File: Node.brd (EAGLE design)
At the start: 27.9 x 27.9 mm, 60 parts, among them J1 DF12A3.0-14DS, Q1 16MHz, U1 ATMEGA32U4QFN, U2 NRF24L01NOPAD, U3 LTC3553, U4 L3GD20, U6 LSM303DLHC, U7 BD2425NNRF0404, U9 RCLAMP0502A, X1 USB-FCI

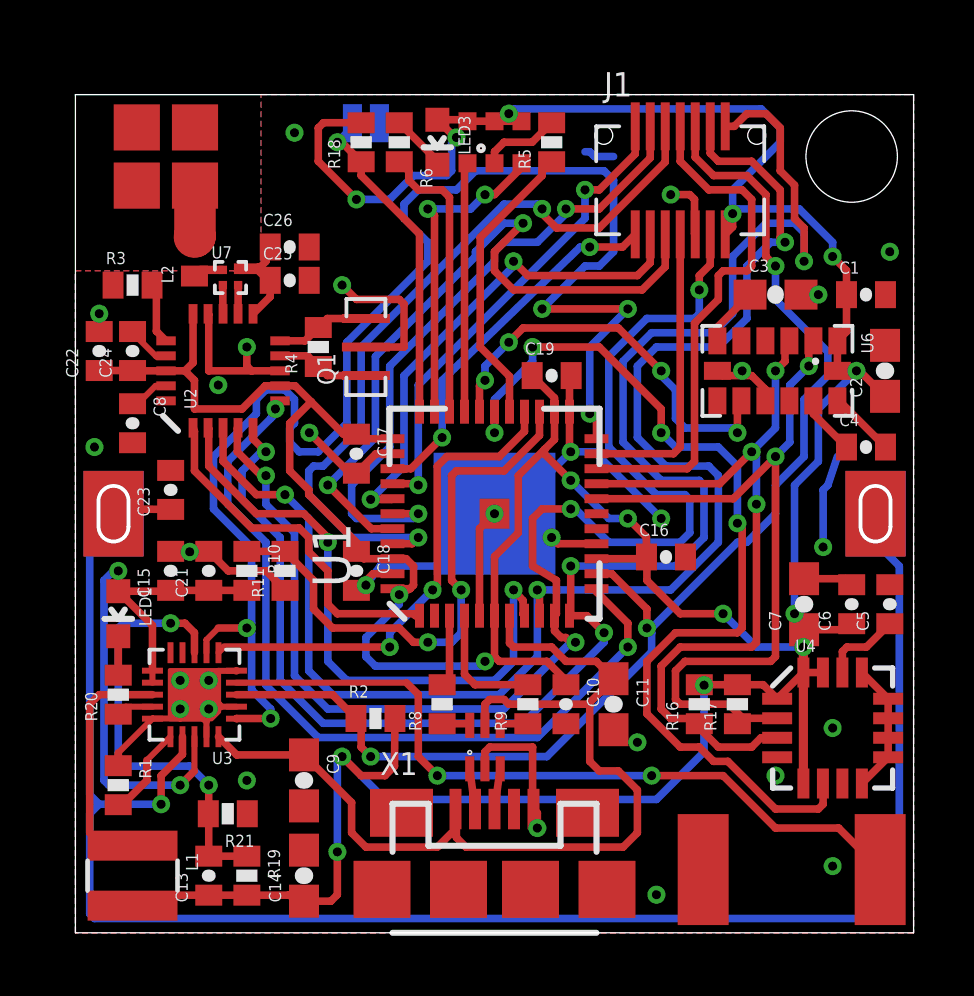
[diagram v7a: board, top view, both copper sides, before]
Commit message: with silkscreen
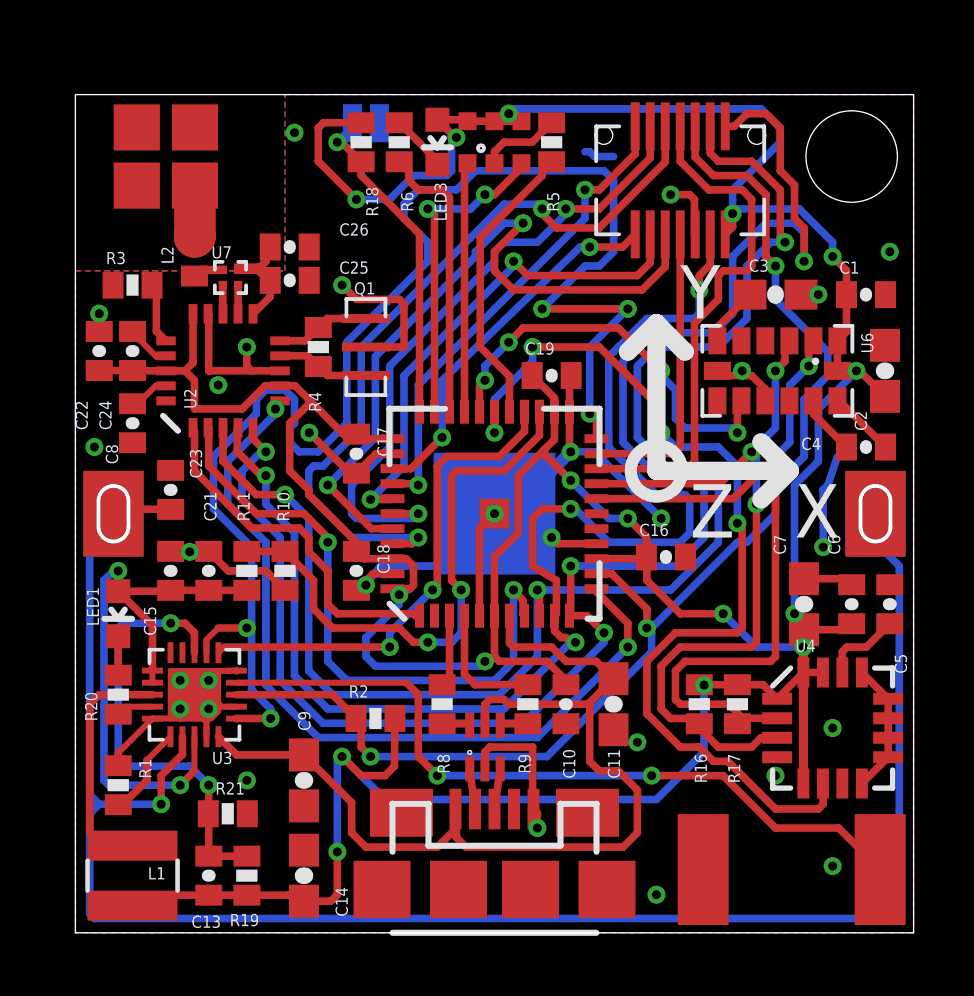
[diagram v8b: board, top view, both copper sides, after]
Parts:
- added U$2: (no value), SparkFun-Aesthetics:OSHW-LOGO-M
- added U$3: (no value), adjacent-reality:ADJACENTREALITY-LOGO-0.35
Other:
- board text added: "Adjacent Reality Tracker 0.3"
- board text added: "CC BY 3.0"
- board text added: "With help from Donald Cober"
- board text added: "X"
- board text added: "Y"
- board text added: "Z"
- board text removed: "Adjacent Reality Tracker 0.2"
- board text removed: "Creative Commons BY-SA 3.0"
- board text removed: "Donald Cober"
